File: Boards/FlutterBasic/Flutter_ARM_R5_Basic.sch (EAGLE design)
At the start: 78 parts, among them U1 MIC5235-3.3, U2 CC1200, U3 SAM3S4/2/1A_48PIN_LQFP, U4 MCP73831, U5 BALUN_CC1200, U6 ATSHA204/ATECC108UDFN, U7 U.FL, X1 12MHz, X2 40MHz

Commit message: Reorganized schematic, generated PDF schematic.
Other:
- note added: "Battery Charging"
- note added: "Buttons"
- note added: "Connectors/GPIO"
- note added: "Crypto"
- note added: "Flutter Basic: SAM3S1A Flutter Pro: SAM3S2A"
- note added: "Flutter is Free/Libre Hardware. Released under the Creative Commons Attribution Share-Alike 4.0 License http://creativecommons.org/licenses/by-sa/4.0/ Designed by: Taylor Alexander of Flutter Wireless, Inc. Copyright Taylor Alexander 2014"
- note added: "LED"
- note added: "Main Processor"
- note added: "Radio"
- note added: "USB"
- note added: "USB Sense"
- note added: "Voltage Input"
- note added: "Voltage Sense"
- note removed: "Released under the Creative Commons Attribution Share-Alike 4.0 License http://creativecommons.org/licenses/by-sa/4.0/ Designed by: Taylor Alexander of Flutter Wireless, Inc. Copyright Taylor Alexander 2014"
- moved on the sheet: C11, C121, C131, C151, C171, C172, C173, C2, C203, C211, C221, C231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

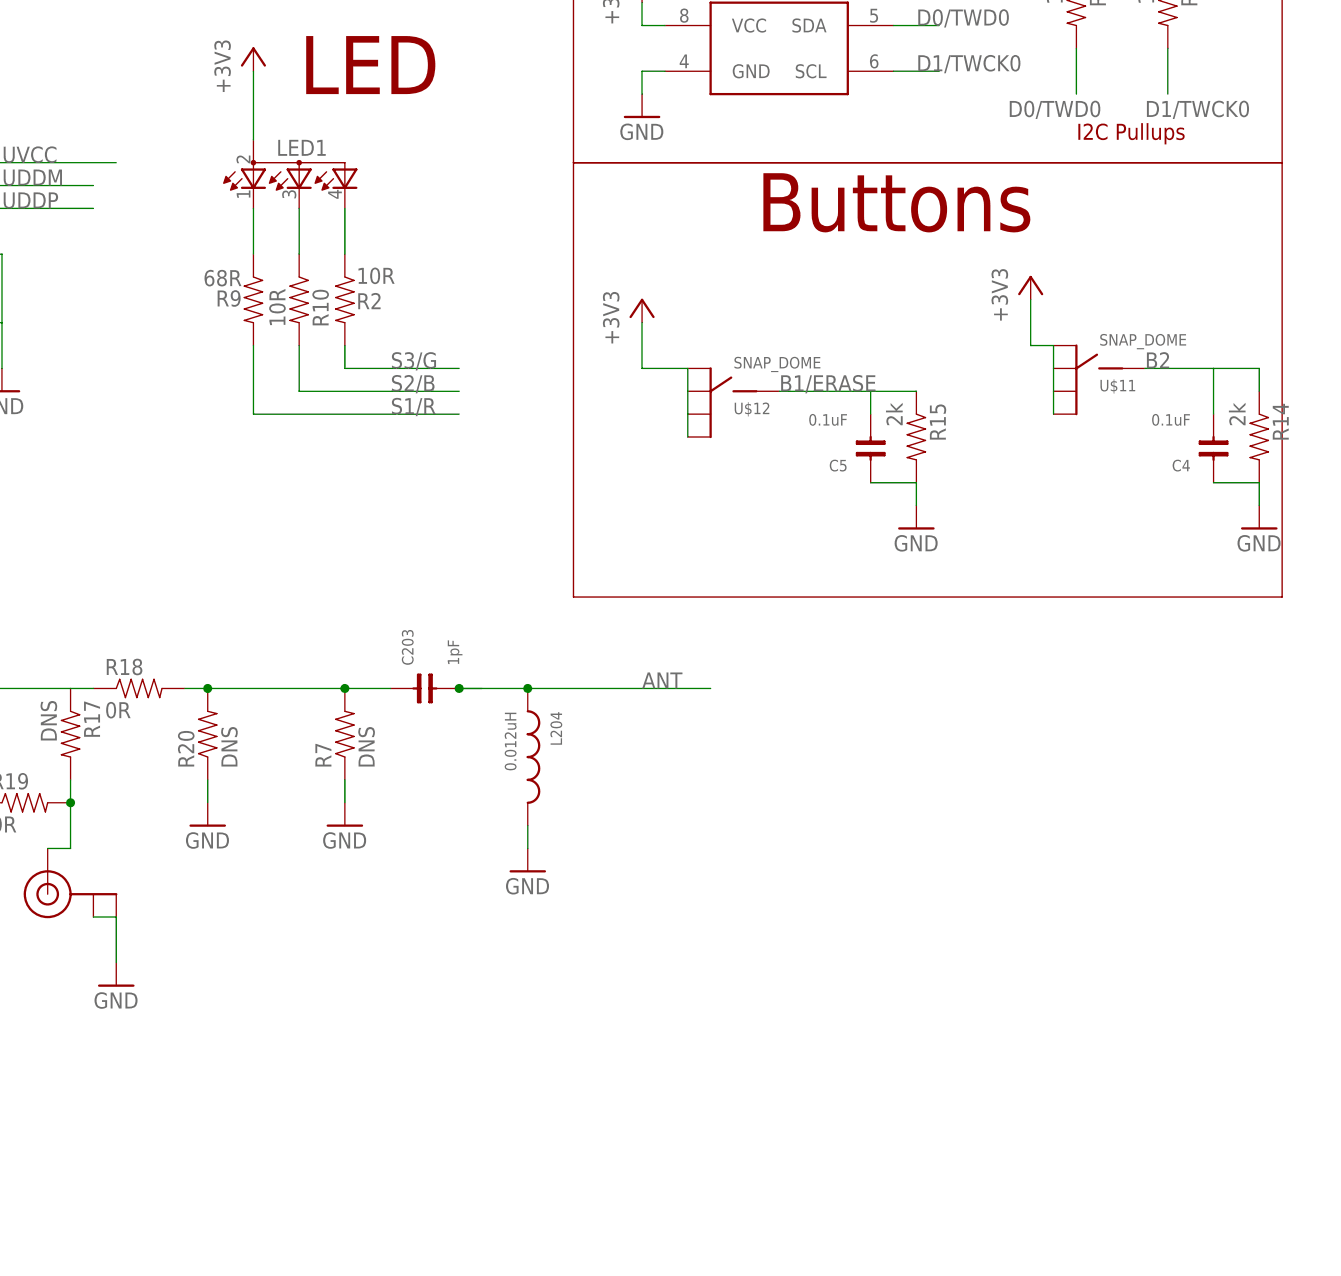
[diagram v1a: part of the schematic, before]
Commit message: Added version number, changed schematic name.
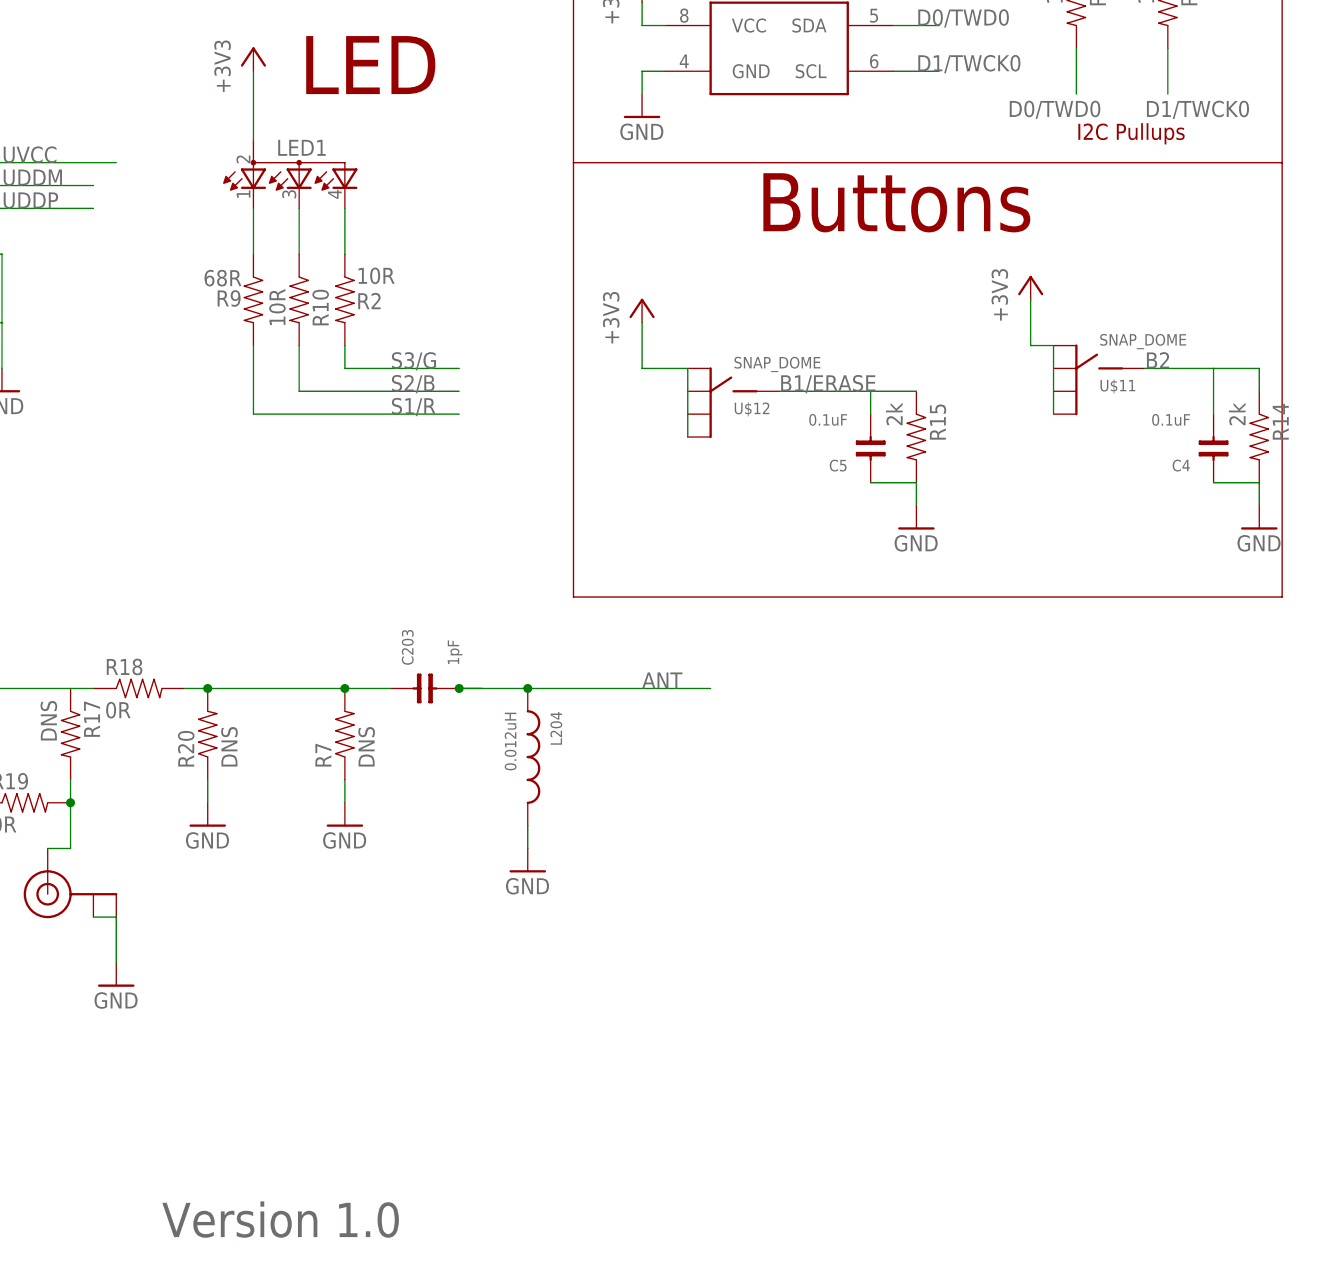
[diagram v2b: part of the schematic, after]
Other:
- note added: "Version 1.0"
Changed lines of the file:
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@@
 <wire x1="299.72" y1="160.02" x2="378.46" y2="160.02" width="0.1524" layer="94"/>
 <wire x1="378.46" y1="160.02" x2="378.46" y2="127" width="0.1524" layer="94"/>
-<wire x1="378.46" y1="127" x2="299.72" y2="127" width="0.1524" layer="94"/>
 <wire x1="299.72" y1="127" x2="299.72" y2="160.02" width="0.1524" layer="94"/>
 <text x="355.6" y="129.54" size="1.778" layer="94">I2C Pullups</text>
@@
 <wire x1="378.46" y1="78.74" x2="299.72" y2="78.74" width="0.1524" layer="94"/>
 <wire x1="299.72" y1="78.74" x2="299.72" y2="127" width="0.1524" layer="94"/>
+<text x="254" y="7.62" size="3.81" layer="95">Version 1.0</text>
 </plain>
 <instances>
